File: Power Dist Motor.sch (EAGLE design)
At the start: 11 parts

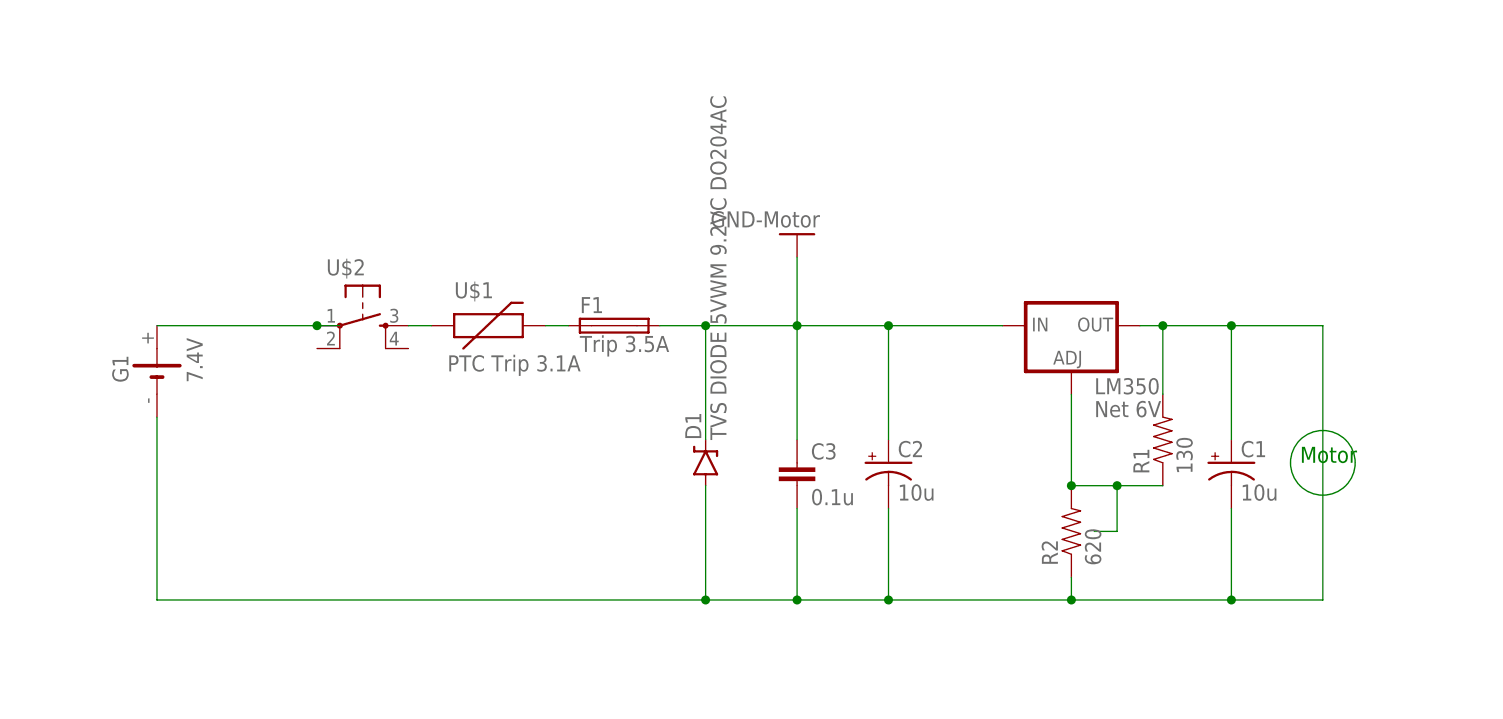
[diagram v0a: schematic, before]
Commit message: Fixed up the schematics and PCBs for power dist
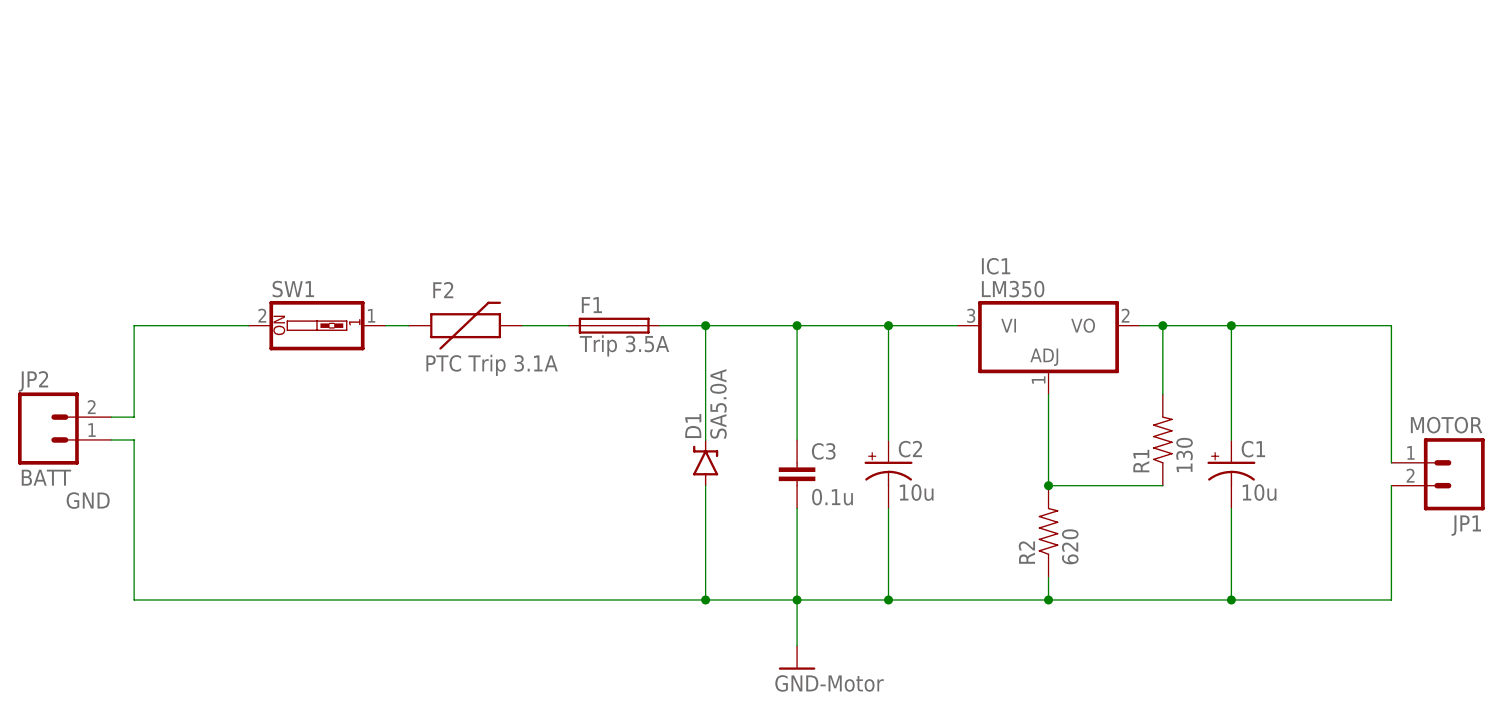
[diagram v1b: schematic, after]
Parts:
- removed G1: 7.4V, battery:SL-340/P3.6V
- removed LM350: Net 6V, SparkFun-PowerIC:V_REG_317DPACK
- removed U$1: PTC Trip 3.1A, GeekAmmo:PTC
- removed U$2: TACTILE-SWITCH-7914G, GeekAmmo:TACTILE-SWITCH-7914G
- added F2: PTC Trip 3.1A, SparkFun-PowerIC:PTCPTH
- added IC1: LM350, linear:317T
- added JP1: MOTOR, SparkFun-Connectors:M02PTH
- added JP2: BATT, SparkFun-Connectors:M02PTH
- added SW1: (no value), special:SW_DIP-1
- C3: device SparkFun-Capacitors:0.1UF-50V-20%(PTH)KIT-EZ -> SparkFun-Capacitors:CAPPTH
- D1: value TVS DIODE 5VWM 9.2VC DO204AC -> SA5.0A
- F1: device fuse:19559 -> fuse:PICOFUSE
- R1, R2: device SparkFun-Resistors:RESISTORPTH-1/2W -> SparkFun-Passives:RESISTORPTH-1/4W
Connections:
- removed net N$8: C1.+, C1.-, C2.-, C3.2, D1.A, G1.-, LM350.OUT, R1.2, R2.1
- new net N$1: C1.+, IC1.VO, JP1.1, R1.2
- new net N$7: C2.+, C3.1, D1.C, F1.2, IC1.VI
- net GND: now also C1.-, C2.-, C3.2, D1.A, JP1.2, JP2.1, R2.1; no longer C2.+, C3.1, D1.C, F1.2, LM350.IN
- net N$2: now also JP2.2, SW1.2; no longer G1.+, U$2.1
- net N$3: now also F2.1, SW1.1; no longer U$1.1, U$2.3
- net N$4: now also IC1.ADJ; no longer LM350.ADJ
- net N$5: now also F2.2; no longer U$1.2
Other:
- note removed: "Motor"
- moved on the sheet: R2
